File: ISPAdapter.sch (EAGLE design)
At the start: 7 parts

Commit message: Tidy
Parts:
- renumbered U$3 to U1
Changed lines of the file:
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@@
 <part name="GND1" library="SparkFun-Aesthetics" deviceset="GND" device=""/>
 <part name="JP3" library="SparkFun-Connectors" deviceset="M01" device="PTH"/>
-<part name="U$3" library="dubec" deviceset="SWITCH_IC_QUAD" device="SN74HC4066PW"/>
+<part name="U1" library="dubec" deviceset="SWITCH_IC_QUAD" device="SN74HC4066PW"/>
 <part name="GND5" library="SparkFun-Aesthetics" deviceset="GND" device=""/>
 <part name="S1" library="SparkFun-Electromechanical" deviceset="SWITCH-SPDT" device="ESWITCH"/>
@@
 <instance part="GND1" gate="1" x="66.04" y="78.74"/>
 <instance part="JP3" gate="G$1" x="45.72" y="91.44" rot="R270"/>
-<instance part="U$3" gate="G$1" x="58.42" y="48.26"/>
+<instance part="U1" gate="G$1" x="58.42" y="48.26"/>
 <instance part="GND5" gate="1" x="43.18" y="35.56"/>
 <instance part="S1" gate="1" x="15.24" y="45.72"/>
@@
 </segment>
 <segment>
-<pinref part="U$3" gate="G$1" pin="VCC"/>
+<pinref part="U1" gate="G$1" pin="VCC"/>
 <wire x1="71.12" y1="55.88" x2="73.66" y2="55.88" width="0.1524" layer="91"/>
 <label x="73.66" y="55.88" size="1.27" layer="95" xref="yes"/>
@@
 </segment>
 <segment>
-<pinref part="U$3" gate="G$1" pin="3B"/>
+<pinref part="U1" gate="G$1" pin="3B"/>
 <wire x1="71.12" y1="43.18" x2="73.66" y2="43.18" width="0.1524" layer="91"/>
 <label x="73.66" y="43.18" size="1.27" layer="95" xref="yes"/>
@@
 </segment>
 <segment>
-<pinref part="U$3" gate="G$1" pin="1B"/>
+<pinref part="U1" gate="G$1" pin="1B"/>
 <wire x1="45.72" y1="53.34" x2="43.18" y2="53.34" width="0.1524" layer="91"/>
 <label x="43.18" y="53.34" size="1.27" layer="95" rot="R180" xref="yes"/>
@@
 </segment>
 <segment>
-<pinref part="U$3" gate="G$1" pin="2B"/>
+<pinref part="U1" gate="G$1" pin="2B"/>
 <wire x1="45.72" y1="50.8" x2="43.18" y2="50.8" width="0.1524" layer="91"/>
 <label x="43.18" y="50.8" size="1.27" layer="95" rot="R180" xref="yes"/>
@@
 </segment>
 <segment>
-<pinref part="U$3" gate="G$1" pin="GND"/>
+<pinref part="U1" gate="G$1" pin="GND"/>
 <wire x1="45.72" y1="40.64" x2="43.18" y2="40.64" width="0.1524" layer="91"/>
 <wire x1="43.18" y1="40.64" x2="43.18" y2="38.1" width="0.1524" layer="91"/>
@@
 </segment>
 <segment>
-<pinref part="U$3" gate="G$1" pin="4C"/>
+<pinref part="U1" gate="G$1" pin="4C"/>
 <wire x1="71.12" y1="50.8" x2="73.66" y2="50.8" width="0.1524" layer="91"/>
 <label x="73.66" y="50.8" size="1.27" layer="95" xref="yes"/>
 </segment>
 <segment>
-<pinref part="U$3" gate="G$1" pin="4A"/>
+<pinref part="U1" gate="G$1" pin="4A"/>
 <wire x1="71.12" y1="48.26" x2="73.66" y2="48.26" width="0.1524" layer="91"/>
 <label x="73.66" y="48.26" size="1.27" layer="95" xref="yes"/>
 </segment>
 <segment>
-<pinref part="U$3" gate="G$1" pin="4B"/>
+<pinref part="U1" gate="G$1" pin="4B"/>
 <wire x1="71.12" y1="45.72" x2="73.66" y2="45.72" width="0.1524" layer="91"/>
 <label x="73.66" y="45.72" size="1.27" layer="95" xref="yes"/>
@@
 <net name="ISP_EN" class="0">
 <segment>
-<pinref part="U$3" gate="G$1" pin="1C"/>
+<pinref part="U1" gate="G$1" pin="1C"/>
 <wire x1="71.12" y1="53.34" x2="73.66" y2="53.34" width="0.1524" layer="91"/>
 <label x="73.66" y="53.34" size="1.27" layer="95" xref="yes"/>
 </segment>
 <segment>
-<pinref part="U$3" gate="G$1" pin="2C"/>
+<pinref part="U1" gate="G$1" pin="2C"/>
 <wire x1="45.72" y1="45.72" x2="43.18" y2="45.72" width="0.1524" layer="91"/>
 <label x="43.18" y="45.72" size="1.27" layer="95" rot="R180" xref="yes"/>
 </segment>
 <segment>
-<pinref part="U$3" gate="G$1" pin="3C"/>
+<pinref part="U1" gate="G$1" pin="3C"/>
 <wire x1="45.72" y1="43.18" x2="43.18" y2="43.18" width="0.1524" layer="91"/>
 <label x="43.18" y="43.18" size="1.27" layer="95" rot="R180" xref="yes"/>
@@
 </segment>
 <segment>
-<pinref part="U$3" gate="G$1" pin="2A"/>
+<pinref part="U1" gate="G$1" pin="2A"/>
 <wire x1="45.72" y1="48.26" x2="43.18" y2="48.26" width="0.1524" layer="91"/>
 <label x="43.18" y="48.26" size="1.27" layer="95" rot="R180" xref="yes"/>
@@
 </segment>
 <segment>
-<pinref part="U$3" gate="G$1" pin="1A"/>
+<pinref part="U1" gate="G$1" pin="1A"/>
 <wire x1="45.72" y1="55.88" x2="43.18" y2="55.88" width="0.1524" layer="91"/>
 <label x="43.18" y="55.88" size="1.27" layer="95" rot="R180" xref="yes"/>
@@
 </segment>
 <segment>
-<pinref part="U$3" gate="G$1" pin="3A"/>
+<pinref part="U1" gate="G$1" pin="3A"/>
 <wire x1="71.12" y1="40.64" x2="73.66" y2="40.64" width="0.1524" layer="91"/>
 <label x="73.66" y="40.64" size="1.27" layer="95" xref="yes"/>

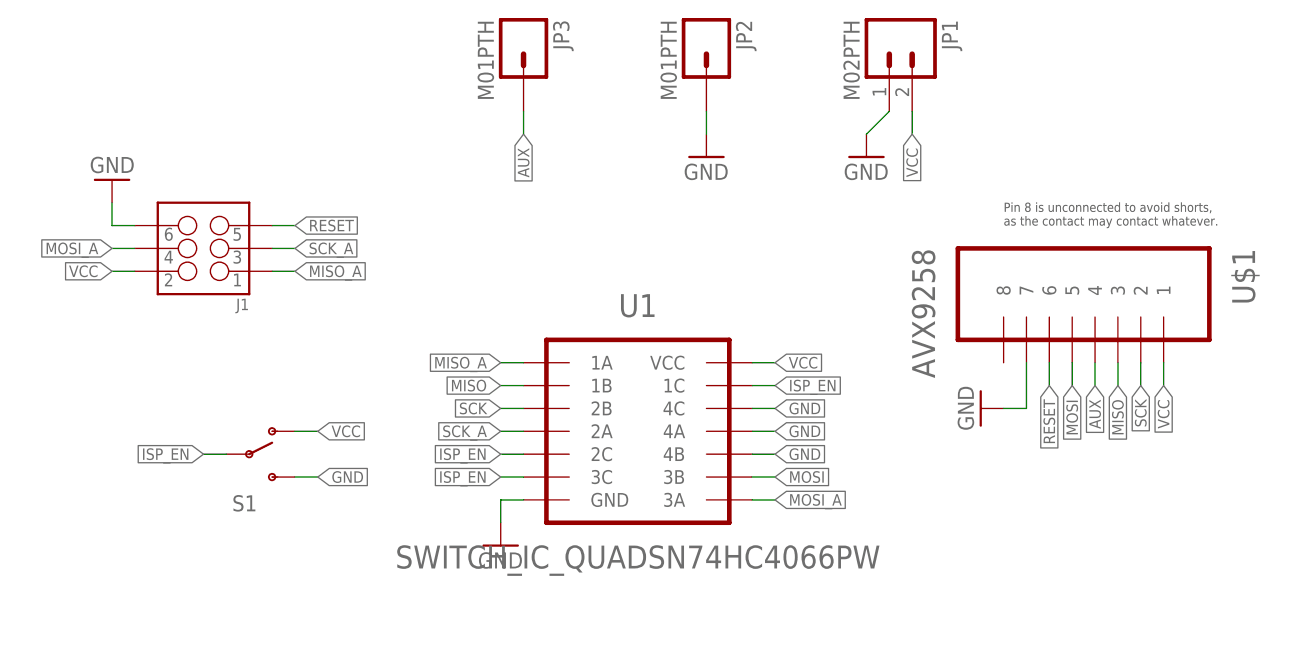
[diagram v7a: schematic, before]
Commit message: Changed switch IC
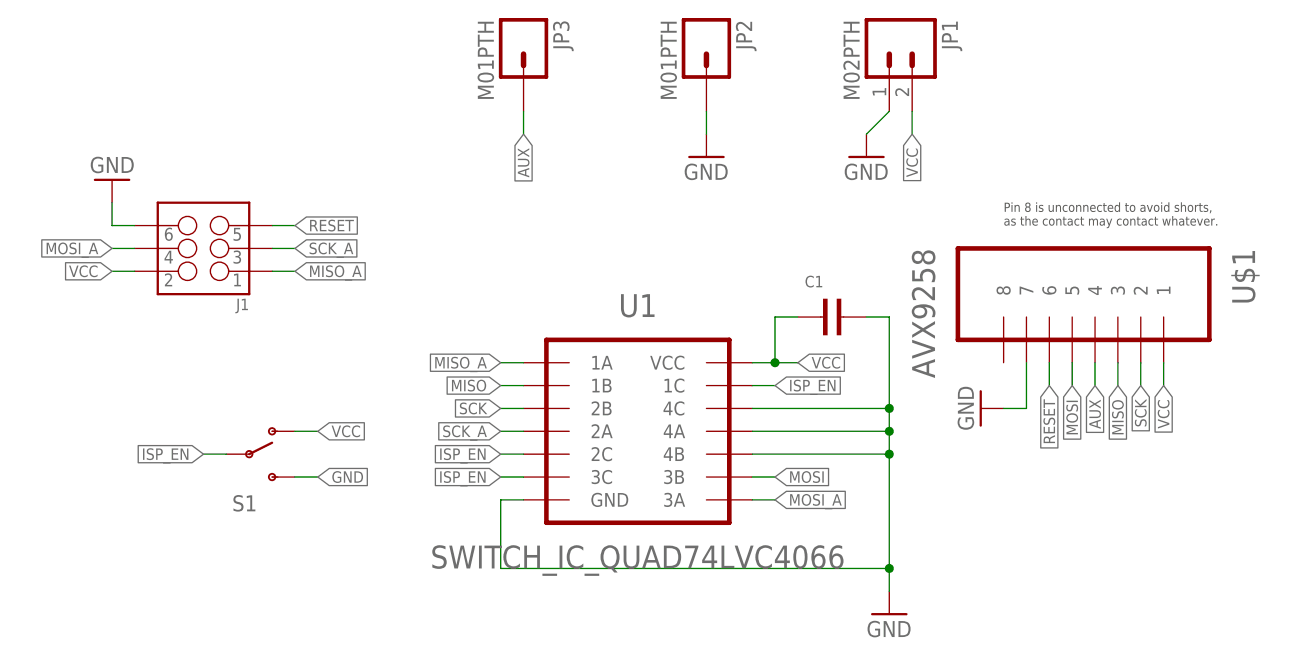
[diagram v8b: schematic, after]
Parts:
- added C1: (no value), dubec:CAP4.7UF_10V
- U1: value SWITCH_IC_QUADSN74HC4066PW -> SWITCH_IC_QUAD74LVC4066; device dubec:SWITCH_IC_QUADSN74HC4066PW -> dubec:SWITCH_IC_QUAD74LVC4066
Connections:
- net DGND: now also C1.2, U1.4A, U1.4B, U1.4C, U1.GND
- net GND: no longer U1.4A, U1.4B, U1.4C, U1.GND
- net VCC: now also C1.1
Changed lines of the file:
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@@
 <part name="GND1" library="SparkFun-Aesthetics" deviceset="GND" device=""/>
 <part name="JP3" library="SparkFun-Connectors" deviceset="M01" device="PTH"/>
-<part name="U1" library="dubec" deviceset="SWITCH_IC_QUAD" device="SN74HC4066PW"/>
-<part name="GND5" library="SparkFun-Aesthetics" deviceset="GND" device=""/>
+<part name="U1" library="dubec" deviceset="SWITCH_IC_QUAD" device="74LVC4066" value="SWITCH_IC_QUAD74LVC4066"/>
 <part name="S1" library="SparkFun-Electromechanical" deviceset="SWITCH-SPDT" device="ESWITCH"/>
+<part name="GND6" library="SparkFun-Aesthetics" deviceset="GND" device=""/>
+<part name="C1" library="dubec" deviceset="CAP" device="4.7UF_10V"/>
 </parts>
 <sheets>
@@
 <instance part="JP3" gate="G$1" x="45.72" y="91.44" rot="R270"/>
 <instance part="U1" gate="G$1" x="58.42" y="48.26"/>
-<instance part="GND5" gate="1" x="43.18" y="35.56"/>
 <instance part="S1" gate="1" x="15.24" y="45.72"/>
+<instance part="GND6" gate="1" x="86.36" y="27.94"/>
+<instance part="C1" gate="G$1" x="78.74" y="60.96"/>
 </instances>
 <busses>
@@
 <pinref part="U1" gate="G$1" pin="VCC"/>
 <wire x1="71.12" y1="55.88" x2="73.66" y2="55.88" width="0.1524" layer="91"/>
-<label x="73.66" y="55.88" size="1.27" layer="95" xref="yes"/>
+<label x="76.2" y="55.88" size="1.27" layer="95" xref="yes"/>
+<pinref part="C1" gate="G$1" pin="1"/>
+<wire x1="73.66" y1="55.88" x2="76.2" y2="55.88" width="0.1524" layer="91"/>
+<wire x1="76.2" y1="60.96" x2="73.66" y2="60.96" width="0.1524" layer="91"/>
+<wire x1="73.66" y1="60.96" x2="73.66" y2="55.88" width="0.1524" layer="91"/>
+<junction x="73.66" y="55.88"/>
 </segment>
 <segment>
@@
 <pinref part="U$1" gate="G$1" pin="7"/>
 <wire x1="101.6" y1="50.8" x2="101.6" y2="55.88" width="0.1524" layer="91"/>
+</segment>
+<segment>
+<pinref part="U1" gate="G$1" pin="GND"/>
+<wire x1="45.72" y1="40.64" x2="43.18" y2="40.64" width="0.1524" layer="91"/>
+</segment>
+<segment>
+<pinref part="GND6" gate="1" pin="GND"/>
+<wire x1="43.18" y1="40.64" x2="43.18" y2="33.02" width="0.1524" layer="91"/>
+<pinref part="U1" gate="G$1" pin="4C"/>
+<wire x1="71.12" y1="50.8" x2="86.36" y2="50.8" width="0.1524" layer="91"/>
+<wire x1="86.36" y1="50.8" x2="86.36" y2="48.26" width="0.1524" layer="91"/>
+<pinref part="U1" gate="G$1" pin="4A"/>
+<wire x1="86.36" y1="48.26" x2="86.36" y2="45.72" width="0.1524" layer="91"/>
+<wire x1="86.36" y1="45.72" x2="86.36" y2="33.02" width="0.1524" layer="91"/>
+<wire x1="86.36" y1="33.02" x2="86.36" y2="30.48" width="0.1524" layer="91"/>
+<wire x1="71.12" y1="48.26" x2="86.36" y2="48.26" width="0.1524" layer="91"/>
+<junction x="86.36" y="48.26"/>
+<pinref part="U1" gate="G$1" pin="4B"/>
+<wire x1="71.12" y1="45.72" x2="86.36" y2="45.72" width="0.1524" layer="91"/>
+<junction x="86.36" y="45.72"/>
+<wire x1="43.18" y1="33.02" x2="86.36" y2="33.02" width="0.1524" layer="91"/>
+<junction x="86.36" y="33.02"/>
+<pinref part="C1" gate="G$1" pin="2"/>
+<wire x1="83.82" y1="60.96" x2="86.36" y2="60.96" width="0.1524" layer="91"/>
+<wire x1="86.36" y1="60.96" x2="86.36" y2="50.8" width="0.1524" layer="91"/>
+<junction x="86.36" y="50.8"/>
 </segment>
 </net>
@@
 </segment>
 <segment>
-<pinref part="U1" gate="G$1" pin="GND"/>
-<wire x1="45.72" y1="40.64" x2="43.18" y2="40.64" width="0.1524" layer="91"/>
-<wire x1="43.18" y1="40.64" x2="43.18" y2="38.1" width="0.1524" layer="91"/>
-<pinref part="GND5" gate="1" pin="GND"/>
-</segment>
-<segment>
-<pinref part="U1" gate="G$1" pin="4C"/>
-<wire x1="71.12" y1="50.8" x2="73.66" y2="50.8" width="0.1524" layer="91"/>
-<label x="73.66" y="50.8" size="1.27" layer="95" xref="yes"/>
-</segment>
-<segment>
-<pinref part="U1" gate="G$1" pin="4A"/>
-<wire x1="71.12" y1="48.26" x2="73.66" y2="48.26" width="0.1524" layer="91"/>
-<label x="73.66" y="48.26" size="1.27" layer="95" xref="yes"/>
-</segment>
-<segment>
-<pinref part="U1" gate="G$1" pin="4B"/>
-<wire x1="71.12" y1="45.72" x2="73.66" y2="45.72" width="0.1524" layer="91"/>
-<label x="73.66" y="45.72" size="1.27" layer="95" xref="yes"/>
-</segment>
-<segment>
